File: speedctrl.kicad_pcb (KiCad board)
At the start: 2 copper layers, 30 parts, among them J1 Conn_01x06, J2 Conn_02x04_Odd_Even, J3 Conn_01x02, Q1 Q_NMOS_GDSD, U1 LM317L_SO8, U2 BD6231, U3 LM317L_SO8, U4 STM32F030F4Px

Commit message: Route PCB
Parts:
- added C13: 10pF, Capacitor_SMD:C_0603_1608Metric, F.Cu at (99.1, 80.0)
- added C14: 10pF, Capacitor_SMD:C_0603_1608Metric, F.Cu at (99.1, 83.3)
- added H1: MountingHole, MountingHole:MountingHole_4.3mm_M4, F.Cu at (95.2, 62.9)
- added H2: MountingHole, MountingHole:MountingHole_4.3mm_M4, F.Cu at (95.2, 91.4)
- added H3: MountingHole, MountingHole:MountingHole_4.3mm_M4, F.Cu at (132.1, 62.9)
- added H4: MountingHole, MountingHole:MountingHole_4.3mm_M4, F.Cu at (132.1, 91.4)
- added Y1: ABM10-16MHz, Crystal:Crystal_SMD_Abracon_ABM10-4Pin_2.5x2.0mm, F.Cu at (95.9, 81.7)
- moved R1 26.7 mm to (124.5, 83.2)
- moved U1 26.5 mm to (125.7, 78.7)
- moved C1 26.3 mm to (124.5, 74.3)
- moved R3 25.9 mm to (120.0, 80.0)
- moved C3 25.9 mm to (120.0, 76.8)
- moved C5 15.8 mm to (95.7, 85.1), turned to 0 degrees
- moved C10 12.9 mm to (115.5, 77.4), turned to 90 degrees
- moved C2 11.7 mm to (101.6, 66.0)
- moved C11 11.0 mm to (117.4, 77.4), turned to 90 degrees
- moved U3 10.9 mm to (101.6, 70.5)
- moved R2 10.2 mm to (99.8, 74.9)
- moved U2 9.09 mm to (114.4, 82.5)
- moved U4 7.96 mm to (104.8, 83.8)
- moved R4 7.70 mm to (96.4, 74.9), turned to 0 degrees
- moved C4 7.65 mm to (95.9, 71.1), turned to 180 degrees
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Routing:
- net +24V: track 0.00 -> 85.4 mm, vias 0 -> 6
- net +3V3: track 0.00 -> 77.9 mm, vias 0 -> 3
- net Net-(Q1-Pad1): track 0.00 -> 35.8 mm, vias 0 -> 4
- net GND: track 0.00 -> 32.3 mm, vias 0 -> 15
- net +16V: track 0.00 -> 29.2 mm
- net /SPEED_POT_SLIDER: track 0.00 -> 24.4 mm
- net /SWCLK: track 0.00 -> 20.5 mm
- net /NRST: track 0.00 -> 19.1 mm
- net /33-45SW: track 0.00 -> 18.8 mm
- net Net-(D1-Pad2): track 0.00 -> 16.6 mm
- net Net-(U2-Pad4): track 0.00 -> 14.0 mm, vias 0 -> 2
- net /SWDIO: track 0.00 -> 12.3 mm
- net Net-(J2-Pad7): track 0.00 -> 11.0 mm
- net Net-(C9-Pad2): track 0.00 -> 7.94 mm
- net Net-(J2-Pad5): track 0.00 -> 7.60 mm
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- added copper zone on B.Cu, net GND
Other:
- board outline added: 45.7 x 37.5 mm
- rule trace_min: 0.2 -> 0.127
- rule via_min_size: 0.4 -> 0.6
- board text added: "(C) 2019 Bruno Kremel"
- board text added: "3V3"
- board text added: "GND"
- board text added: "M303 motor driver"
- board text added: "M~~"
- board text added: "Ne HV+"
- board text added: "POT"
- board text added: "SW"
- board text added: "SWCLK"
- board text added: "SWD"
- board text added: "VCC"
- board text added: "VIN"
- board text added: "nRST"

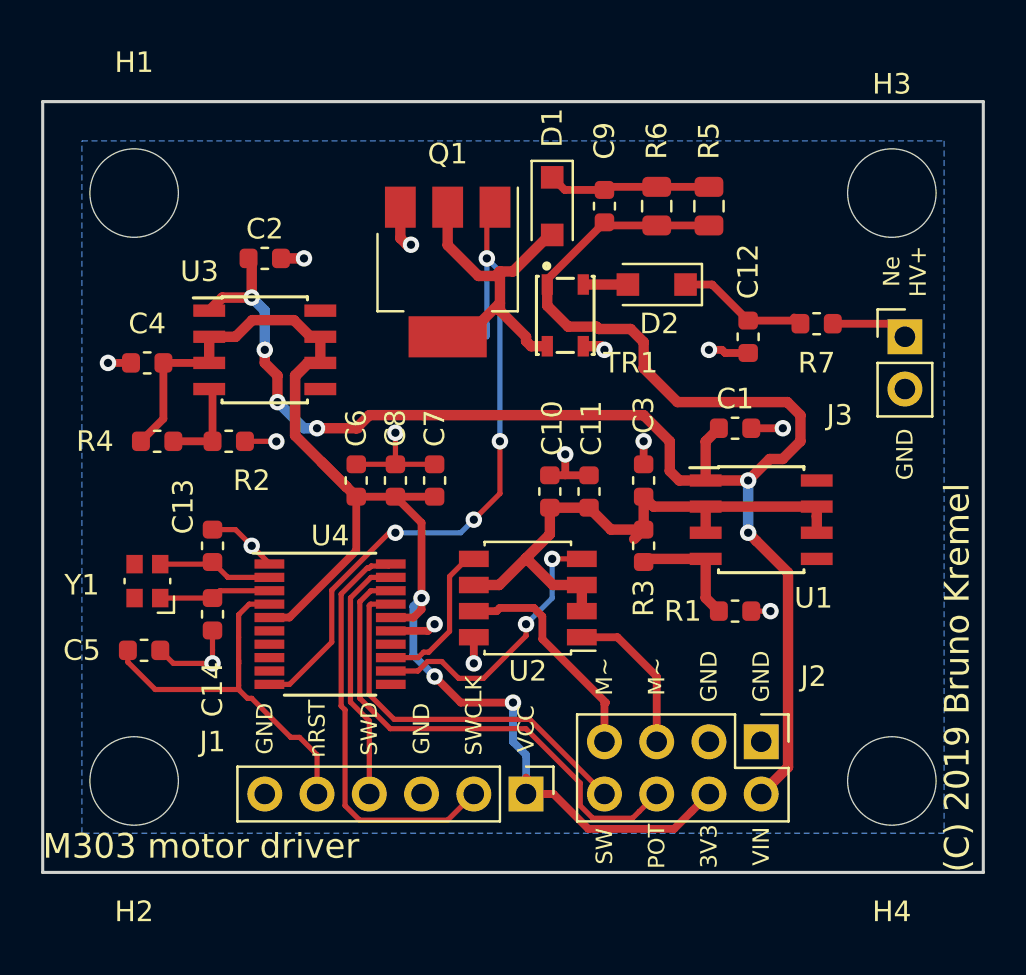
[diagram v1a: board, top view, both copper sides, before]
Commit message: Use DRV8816 instead of the original driver, use BSS138 for flyback
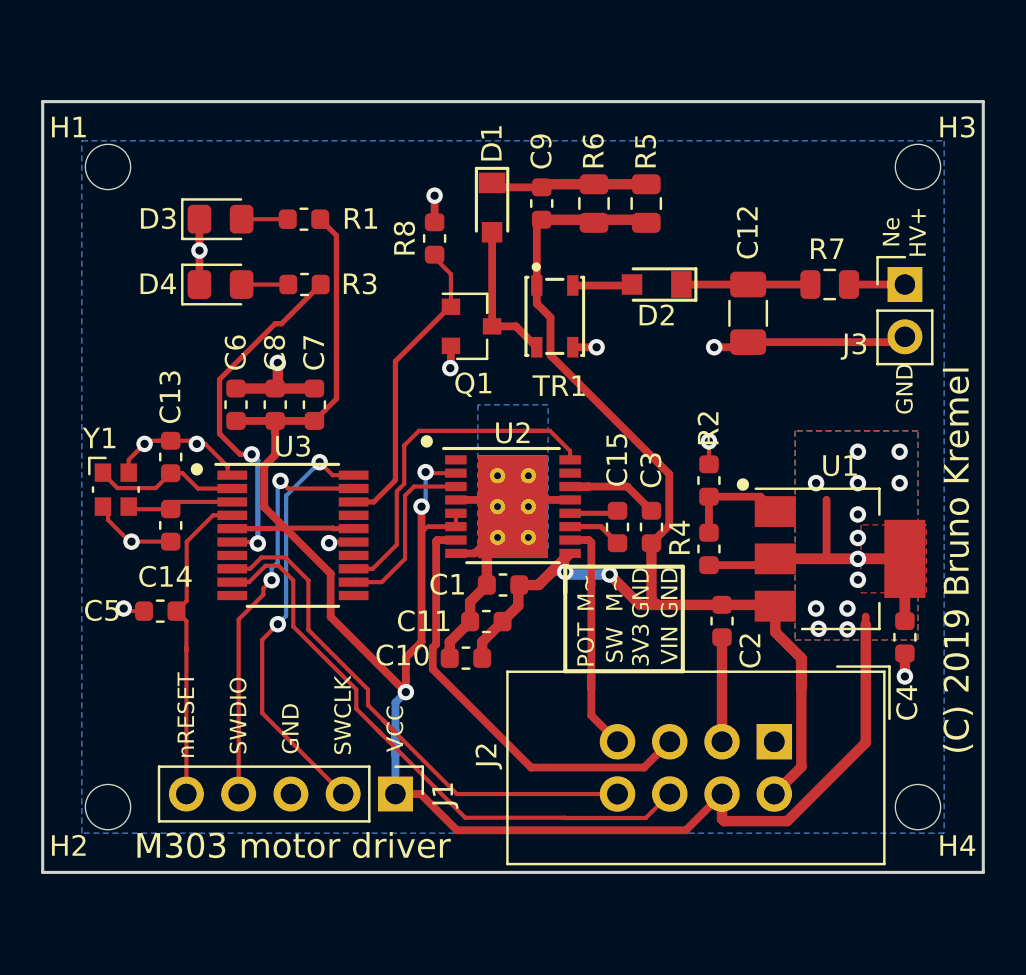
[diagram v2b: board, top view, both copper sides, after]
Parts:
- removed U4: STM32F030F4Px, Package_SO:TSSOP-20_4.4x6.5mm_P0.65mm
- added C15: 100n, Capacitor_SMD:C_0603_1608Metric, F.Cu at (118.7, 79.1)
- added D3: HSMY-C170, LED_SMD:LED_0805_2012Metric_Pad1.15x1.40mm_HandSolder, F.Cu at (99.5, 64.1)
- added D4: HSMG-C170, LED_SMD:LED_0805_2012Metric_Pad1.15x1.40mm_HandSolder, F.Cu at (99.5, 67.3)
- added R8: 10k, Resistor_SMD:R_0603_1608Metric, F.Cu at (109.9, 65.1)
- C1: value 1u -> 100n
- C12: footprint Capacitor_SMD:C_0603_1608Metric -> Capacitor_SMD:C_1206_3216Metric
- C3: value 4u7 -> 100n
- D1, D2: value NHP220S -> DA2JF8100L; footprint Diode_SMD:D_SOD-123F -> speedctrl-footprints:Diode_SMini2-F5-B
- H1, H2, H3, H4: footprint MountingHole:MountingHole_4.3mm_M4 -> MountingHole:MountingHole_2.2mm_M2
- J1: value Conn_01x06 -> Conn_01x05; footprint Connector_PinHeader_2.54mm:PinHeader_1x06_P2.54mm_Vertical -> Connector_PinHeader_2.54mm:PinHeader_1x05_P2.54mm_Vertical
- J2: footprint Connector_PinHeader_2.54mm:PinHeader_2x04_P2.54mm_Vertical -> Connector_IDC:IDC-Header_2x04_P2.54mm_Vertical
- Q1: value Q_NMOS_GDSD -> BSS138; footprint Package_TO_SOT_SMD:SOT-223 -> Package_TO_SOT_SMD:SOT-23
- R1: value 1k8 -> 330
- R2: value 820 -> 560
- R3: value 150 -> 330
- R4: value 270 -> 330
- R7: footprint Resistor_SMD:R_0603_1608Metric -> Resistor_SMD:R_0805_2012Metric
- U1: value LM317L_SO8 -> LM317_3PinPackage; footprint Package_SO:SOIC-8_3.9x4.9mm_P1.27mm -> Package_TO_SOT_SMD:SOT-223-3_TabPin2
- U2: value BD6231 -> DRV8816PWPR; footprint Package_SO:SSOP-8_3.95x5.21x3.27mm_P1.27mm -> Package_SO:HTSSOP-16-1EP_4.4x5mm_P0.65mm_EP3.4x5mm_Mask2.46x2.31mm_ThermalVias
- U3: value LM317L_SO8 -> STM32F070F6Px; footprint Package_SO:SOIC-8_3.9x4.9mm_P1.27mm -> Package_SO:TSSOP-20_4.4x6.5mm_P0.65mm
- Y1: value ABM10-16MHz -> Crystal_GND24
- moved C4 39.2 mm to (132.7, 84.5), turned to 270 degrees
- moved C2 28.4 mm to (123.8, 83.7), turned to 270 degrees
- moved R1 28.3 mm to (103.5, 64.1)
- moved R4 27.3 mm to (123.2, 80.2), turned to 90 degrees
- moved R2 23.4 mm to (123.2, 76.8), turned to 90 degrees
- moved R3 20.8 mm to (103.5, 67.3), turned to 180 degrees
- moved C1 13.6 mm to (113.2, 81.9), turned to 180 degrees
- moved U3 9.12 mm to (103.0, 79.5)
- moved C10 9.07 mm to (111.4, 85.5), turned to 180 degrees
- moved C11 8.06 mm to (112.4, 83.7), turned to 180 degrees
- moved C6 6.91 mm to (100.2, 73.2)
- moved C7 6.91 mm to (104.0, 73.2)
- moved C8 6.91 mm to (102.1, 73.2)
- moved J1 6.35 mm to (108.0, 92.1)
- moved C13 4.77 mm to (97.0, 75.7)
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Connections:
- C10 pad 1: +16V -> +24V
- C11 pad 1: +16V -> +24V
- C3 pad 1: +16V -> +24V
- C3 pad 2: GND -> Net-(C3-Pad2)
- C5 pad 1: /NRST -> Net-(C5-Pad1)
- J1 pad 5: /NRST -> Net-(C5-Pad1)
- J2 pad 6: /SPEED_POT_SLIDER -> /33-45SW
- J2 pad 8: /33-45SW -> /SPEED_POT_SLIDER
- Q1 pad 2: Net-(D1-Pad2) -> GND
- Q1 pad 3: GND -> Net-(D1-Pad2)
- R1 pad 1: Net-(R1-Pad1) -> Net-(D3-Pad2)
- R1 pad 2: GND -> +3V3
- R3 pad 1: +16V -> Net-(R3-Pad1)
- R3 pad 2: Net-(R1-Pad1) -> Net-(D4-Pad2)
- U1 pad 1: +24V -> Net-(R2-Pad1)
- U1 pad 2: +16V -> +3V3
- U1 pad 3: +16V -> +24V
- U2 pad 1: Net-(J2-Pad5) -> (no net)
- U2 pad 2: +16V -> +3V3
- U2 pad 3: +16V -> Net-(U2-Pad3)
- U2 pad 4: Net-(U2-Pad4) -> GND
- U2 pad 5: Net-(U2-Pad5) -> +3V3
- U2 pad 6: +16V -> +3V3
- U2 pad 7: Net-(J2-Pad7) -> Net-(J2-Pad5)
- U3 pad 1: +24V -> GND
- U3 pad 2: +3V3 -> Net-(C13-Pad1)
- U3 pad 3: +3V3 -> Net-(C14-Pad1)
- U3 pad 4: Net-(R2-Pad1) -> Net-(C5-Pad1)
- U3 pad 5: Net-(U3-Pad5) -> +3V3
- U3 pad 6: +3V3 -> Net-(R3-Pad1)
- U3 pad 7: +3V3 -> (no net)
- U3 pad 8: Net-(U3-Pad8) -> /SPEED_POT_SLIDER
- Y1 pad 1: Net-(C14-Pad1) -> Net-(C13-Pad1)
- Y1 pad 2: Net-(C13-Pad1) -> GND
- Y1 pad 3: (no net) -> Net-(C14-Pad1)
- Y1 pad 4: (no net) -> GND
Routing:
- net +3V3: track 77.9 -> 118.7 mm, vias 3 -> 16
- net GND: track 32.3 -> 63.7 mm, vias 15 -> 13
- net +16V: track 29.2 -> 0.00 mm
- net +24V: track 85.4 -> 62.4 mm, vias 6 -> 2
- net Net-(Q1-Pad1): track 35.8 -> 14.8 mm, vias 4 -> 0
- net /NRST: track 19.1 -> 0.00 mm
- net Net-(U2-Pad16): track 0.00 -> 18.7 mm
- net Net-(R3-Pad1): track 0.00 -> 17.2 mm, vias 0 -> 2
- net Net-(C5-Pad1): track 0.00 -> 15.6 mm
- net Net-(U2-Pad4): track 14.0 -> 0.00 mm, vias 2 -> 0
- net Net-(J2-Pad5): track 7.60 -> 21.3 mm
- net /33-45SW: track 18.8 -> 29.5 mm
- net Net-(D1-Pad2): track 16.6 -> 7.17 mm
- net Net-(U2-Pad3): track 0.00 -> 8.87 mm
- net Net-(U2-Pad5): track 7.59 -> 0.00 mm
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- added copper zone on B.Cu, net +3V3
- added copper zone on F.Cu, net +3V3
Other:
- board text added: "SWDIO"
- board text added: "nRESET"
- board text removed: "SWD"
- board text removed: "nRST"
